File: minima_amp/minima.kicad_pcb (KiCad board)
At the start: 2 copper layers, 78 x 60 mm, 40 parts, among them J1 input, J2 output, J3 powersupply, U1 LM1875

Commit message: Pad update and LOGO fix
Updated sizes of pads. Some are bigger while keeping the necessary separations.
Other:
- board text added: "REAL TIME CONSULTING"
- board text removed: "Real-Time Consulting"
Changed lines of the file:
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@@
-(kicad_pcb (version 20171130) (host pcbnew 5.0.0-fee4fd1~66~ubuntu16.04.1)
+(kicad_pcb (version 20171130) (host pcbnew "(5.0.0)")
   (general
     (thickness 1.6)
@@
   )
   (layers
-    (0 F.Cu signal hide)
-    (31 B.Cu signal hide)
-    (32 B.Adhes user hide)
-    (33 F.Adhes user hide)
-    (34 B.Paste user hide)
-    (35 F.Paste user hide)
-    (36 B.SilkS user hide)
+    (0 F.Cu signal)
+    (31 B.Cu signal)
+    (32 B.Adhes user)
+    (33 F.Adhes user)
+    (34 B.Paste user)
+    (35 F.Paste user)
+    (36 B.SilkS user)
     (37 F.SilkS user)
-    (38 B.Mask user hide)
+    (38 B.Mask user)
     (39 F.Mask user)
-    (40 Dwgs.User user hide)
-    (41 Cmts.User user hide)
-    (42 Eco1.User user hide)
-    (43 Eco2.User user hide)
+    (40 Dwgs.User user)
+    (41 Cmts.User user)
+    (42 Eco1.User user)
+    (43 Eco2.User user)
     (44 Edge.Cuts user)
     (45 Margin user)
-    (46 B.CrtYd user hide)
-    (47 F.CrtYd user hide)
-    (48 B.Fab user hide)
-    (49 F.Fab user hide)
+    (46 B.CrtYd user)
+    (47 F.CrtYd user)
+    (48 B.Fab user)
+    (49 F.Fab user)
   )
   (setup
-    (last_trace_width 1.27)
+    (last_trace_width 0.508)
     (user_trace_width 0.508)
     (user_trace_width 0.762)
@@
     (mod_text_size 1 1)
     (mod_text_width 0.15)
-    (pad_size 2.54 2.54)
-    (pad_drill 1.2)
+    (pad_size 3.6 3.3)
+    (pad_drill 1.6)
     (pad_to_mask_clearance 0.2)
     (aux_axis_origin 106.56 45.72)
@@
       (effects (font (size 1 1) (thickness 0.15)))
     )
-    (pad 1 thru_hole circle (at 0 0) (size 3.2 3.2) (drill 1.6) (layers *.Cu *.Mask)
+    (pad 1 thru_hole roundrect (at 0 0) (size 3.6 3.3) (drill 1.6) (layers *.Cu *.Mask) (roundrect_rratio 0.25)
       (net 13 "Net-(C2-Pad2)"))
-    (pad 2 thru_hole roundrect (at 15.24 0) (size 3.3 3.3) (drill 1.6) (layers *.Cu *.Mask) (roundrect_rratio 0.25)
+    (pad 2 thru_hole roundrect (at 15.24 0) (size 3.6 3.3) (drill 1.6) (layers *.Cu *.Mask) (roundrect_rratio 0.25)
       (net 11 /spkhot))
     (model ${KISYS3DMOD}/Inductor_THT.3dshapes/L_Axial_L12.0mm_D5.0mm_P15.24mm_Horizontal_Fastron_MISC.wrl
@@
       (effects (font (size 1 1) (thickness 0.15)))
     )
-    (pad 1 thru_hole rect (at 0 0) (size 2.6 2.6) (drill 1.1) (layers *.Cu *.Mask)
+    (pad 1 thru_hole rect (at 0 0) (size 2.4 2.6) (drill 1.1) (layers *.Cu *.Mask)
       (net 5 "Net-(R1-Pad1)"))
-    (pad 2 thru_hole roundrect (at 1.7 -3.7) (size 2.6 2.6) (drill 1.1) (layers *.Cu *.Mask) (roundrect_rratio 0.25)
+    (pad 2 thru_hole roundrect (at 1.7 -3.7) (size 2.4 2.6) (drill 1.1) (layers *.Cu *.Mask) (roundrect_rratio 0.25)
       (net 17 "Net-(R10-Pad1)"))
-    (pad 3 thru_hole roundrect (at 3.4 0) (size 2.6 2.6) (drill 1.1) (layers *.Cu *.Mask) (roundrect_rratio 0.25)
+    (pad 3 thru_hole roundrect (at 3.4 0) (size 2.4 2.6) (drill 1.1) (layers *.Cu *.Mask) (roundrect_rratio 0.25)
       (net 3 VEE) (zone_connect 2))
-    (pad 4 thru_hole roundrect (at 5.1 -3.7) (size 2.6 2.6) (drill 1.1) (layers *.Cu *.Mask) (roundrect_rratio 0.25)
+    (pad 4 thru_hole roundrect (at 5.1 -3.7) (size 2.4 2.6) (drill 1.1) (layers *.Cu *.Mask) (roundrect_rratio 0.25)
       (net 13 "Net-(C2-Pad2)") (zone_connect 2))
-    (pad 5 thru_hole roundrect (at 6.8 0) (size 2.6 2.6) (drill 1.1) (layers *.Cu *.Mask) (roundrect_rratio 0.25)
+    (pad 5 thru_hole roundrect (at 6.8 0) (size 2.4 2.6) (drill 1.1) (layers *.Cu *.Mask) (roundrect_rratio 0.25)
       (net 2 VCC) (zone_connect 2))
     (model ${KISYS3DMOD}/Package_TO_SOT_THT.3dshapes/TO-220-5_P3.4x3.7mm_StaggerOdd_Lead3.8mm_Vertical.wrl
@@
       (effects (font (size 1 1) (thickness 0.15)))
     )
-    (pad 1 thru_hole rect (at 0 0) (size 3.6 4) (drill 1.4) (layers *.Cu *.Mask)
+    (pad 1 thru_hole rect (at 0 0) (size 3.6 5) (drill 1.4) (layers *.Cu *.Mask)
       (net 3 VEE))
-    (pad 2 thru_hole roundrect (at 5.08 0) (size 3.6 4) (drill 1.4) (layers *.Cu *.Mask) (roundrect_rratio 0.25)
+    (pad 2 thru_hole roundrect (at 5.08 0) (size 3.6 5) (drill 1.4) (layers *.Cu *.Mask) (roundrect_rratio 0.25)
       (net 1 GNDPWR))
-    (pad 3 thru_hole roundrect (at 10.16 0) (size 3.6 4) (drill 1.4) (layers *.Cu *.Mask) (roundrect_rratio 0.25)
+    (pad 3 thru_hole roundrect (at 10.16 0) (size 3.6 5) (drill 1.4) (layers *.Cu *.Mask) (roundrect_rratio 0.25)
       (net 2 VCC))
     (model ${KISYS3DMOD}/TerminalBlock_Phoenix.3dshapes/TerminalBlock_Phoenix_MKDS-3-3-5.08_1x03_P5.08mm_Horizontal.wrl
@@
       (effects (font (size 1 1) (thickness 0.15)))
     )
-    (pad 1 thru_hole rect (at 0 0) (size 2.54 2.54) (drill 1.2) (layers *.Cu *.Mask)
+    (pad 1 thru_hole rect (at 0 0) (size 2.54 3) (drill 1.2) (layers *.Cu *.Mask)
       (net 12 /inp))
-    (pad 2 thru_hole roundrect (at 3.5 0) (size 2.54 2.54) (drill 1.2) (layers *.Cu *.Mask) (roundrect_rratio 0.25)
+    (pad 2 thru_hole roundrect (at 3.5 0) (size 2.54 3) (drill 1.2) (layers *.Cu *.Mask) (roundrect_rratio 0.25)
       (net 10 /sgnd))
-    (pad 3 thru_hole roundrect (at 7 0) (size 2.54 2.54) (drill 1.2) (layers *.Cu *.Mask) (roundrect_rratio 0.25)
+    (pad 3 thru_hole roundrect (at 7 0) (size 2.54 3) (drill 1.2) (layers *.Cu *.Mask) (roundrect_rratio 0.25)
       (net 1 GNDPWR))
     (model ${KISYS3DMOD}/TerminalBlock_Phoenix.3dshapes/TerminalBlock_Phoenix_PT-1,5-3-3.5-H_1x03_P3.50mm_Horizontal.wrl
@@
     (effects (font (size 2.2 2.2) (thickness 0.4)))
   )
-  (gr_text "Real-Time\nConsulting" (at 167.785 87.695 270) (layer B.Cu)
-    (effects (font (size 2 1.7) (thickness 0.4)) (justify mirror))
+  (gr_text " REAL TIME\nCONSULTING" (at 167.785 87.695 270) (layer B.Cu)
+    (effects (font (size 2 1.5) (thickness 0.375)) (justify mirror))
   )
   (gr_text "Minima V1.1" (at 145.56 90.87) (layer F.SilkS)

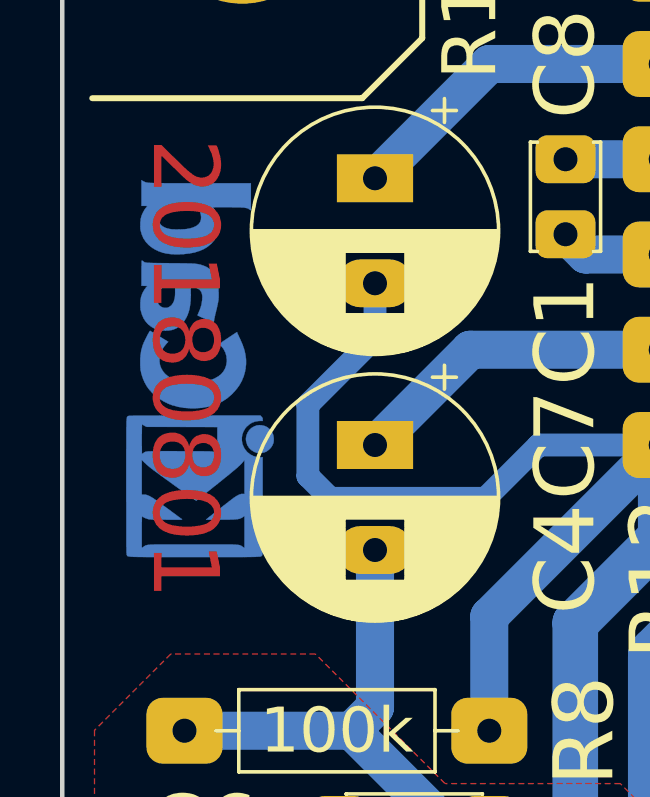
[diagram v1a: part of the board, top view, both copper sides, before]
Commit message: Added hole dimensions to PCB
Added mounting hole space dimensions.
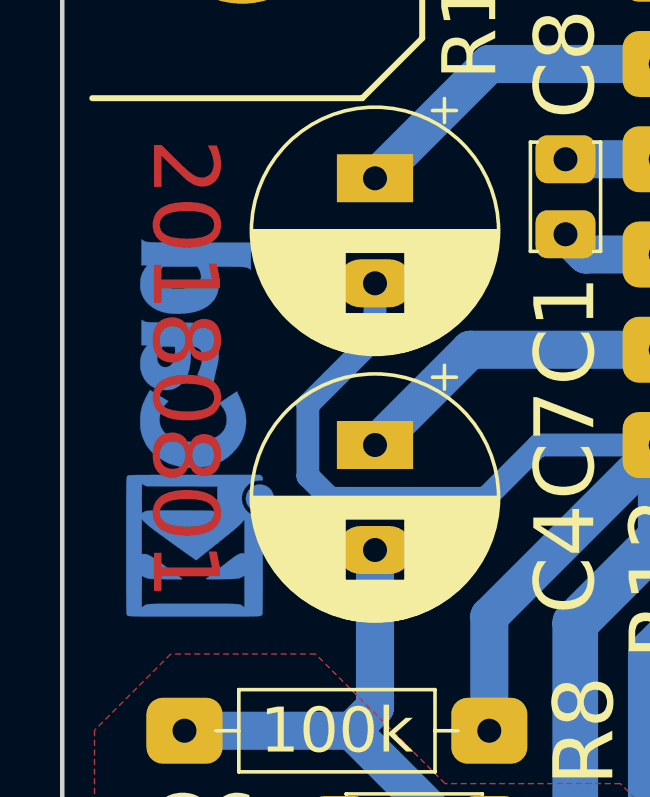
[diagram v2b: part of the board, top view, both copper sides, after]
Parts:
- moved LOGO1 1.98 mm to (110.6, 68.7)
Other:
- board text added: "48"
- board text added: "66"
- board text added: "PG/G/in"
- board text added: "SPK/G"
- board text added: "Vcc/G/Vee"
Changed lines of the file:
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@@
   (general
     (thickness 1.6)
-    (drawings 41)
+    (drawings 58)
     (tracks 115)
     (zones 0)
@@
     (pad_to_mask_clearance 0.2)
     (aux_axis_origin 106.56 45.72)
-    (grid_origin 145.56 54.04)
+    (grid_origin 106.56 45.72)
     (visible_elements 7FFFFFFF)
     (pcbplotparams
@@
   )
   (module Symbol:KiCad-Logo_5mm_Copper (layer B.Cu)
-    (at 110.635 66.74 90)
+    (at 110.635 68.72 90)
     (descr "KiCad Logo")
     (tags "Logo KiCad")
@@
     )
   )
+  (gr_line (start 112.56 93.72) (end 112.56 95.72) (layer B.SilkS) (width 0.2))
+  (gr_line (start 118.56 99.72) (end 116.56 99.72) (layer B.SilkS) (width 0.2))
+  (gr_line (start 174.56 99.72) (end 172.56 99.72) (layer B.SilkS) (width 0.2))
+  (gr_line (start 178.56 95.72) (end 178.56 93.72) (layer B.SilkS) (width 0.2))
+  (gr_line (start 178.56 57.72) (end 178.56 55.72) (layer B.SilkS) (width 0.2))
+  (gr_line (start 174.56 51.72) (end 172.56 51.72) (layer B.SilkS) (width 0.2))
+  (gr_text 66 (at 114.06 57.72 270) (layer B.SilkS)
+    (effects (font (size 1.5 1.5) (thickness 0.3)) (justify mirror))
+  )
+  (gr_line (start 112.56 60.72) (end 112.56 55.72) (layer B.SilkS) (width 0.2))
+  (gr_text 48 (at 118.56 50.22) (layer B.SilkS)
+    (effects (font (size 1.5 1.5) (thickness 0.3)) (justify mirror))
+  )
+  (gr_line (start 116.56 51.72) (end 121.56 51.72) (layer B.SilkS) (width 0.2))
+  (gr_circle (center 112.56 51.72) (end 108.56 51.72) (layer B.SilkS) (width 0.2))
+  (gr_circle (center 112.56 99.72) (end 108.56 99.72) (layer B.SilkS) (width 0.2))
+  (gr_circle (center 178.56 99.72) (end 174.56 99.72) (layer B.SilkS) (width 0.2))
+  (gr_circle (center 178.56 51.72) (end 174.56 51.72) (layer B.SilkS) (width 0.2))
+  (gr_text SPK/G (at 167.912 103.57) (layer B.SilkS)
+    (effects (font (size 1.5 1.5) (thickness 0.3)) (justify mirror))
+  )
+  (gr_text PG/G/in (at 123.716 102.554) (layer B.SilkS)
+    (effects (font (size 1.5 1.5) (thickness 0.3)) (justify mirror))
+  )
+  (gr_text Vcc/G/Vee (at 145.56 94.426) (layer B.SilkS)
+    (effects (font (size 1.5 1.5) (thickness 0.3)) (justify mirror))
+  )
   (gr_text "-|G|+\n24V" (at 158.06 99.72) (layer F.SilkS)
